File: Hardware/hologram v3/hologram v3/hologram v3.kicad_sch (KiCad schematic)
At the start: 706 parts, among them J1 Conn_01x06, J2 Conn_01x06_Socket, SW1 SW_Reset, SW2 SW_Boot, SW3 SW_OPT1, SW4 SW_OPT2, U1 SM16106SC, U10 SM16106SC, U11 SM16106SC, U12 SM16106SC, U13 SM16106SC, U14 SM16106SC, U15 SM16106SC, U16 SM16106SC, U17 SM16106SC, U18 SM16106SC, U19 SM16106SC, U2 SM16106SC, U20 SM16106SC, U21 SM16106SC, U22 SM16106SC, U23 SM16106SC, U24 SM16106SC, U25 SM16106SC, U26 SM16106SC, U27 SM16106SC, U28 SM16106SC, U29 SM16106SC, U3 SM16106SC, U30 SM16106SC, U31 SM16106SC, U32 SM16106SC, U33 ESP32-S3-WROOM-1(N16R8), U34 SY8286ARAC 12v->4v, U36 SY8286ARAC 12v->3.3v, U4 SM16106SC, U5 SM16106SC, U6 SM16106SC, U7 SM16106SC, U8 SM16106SC, U9 SM16106SC

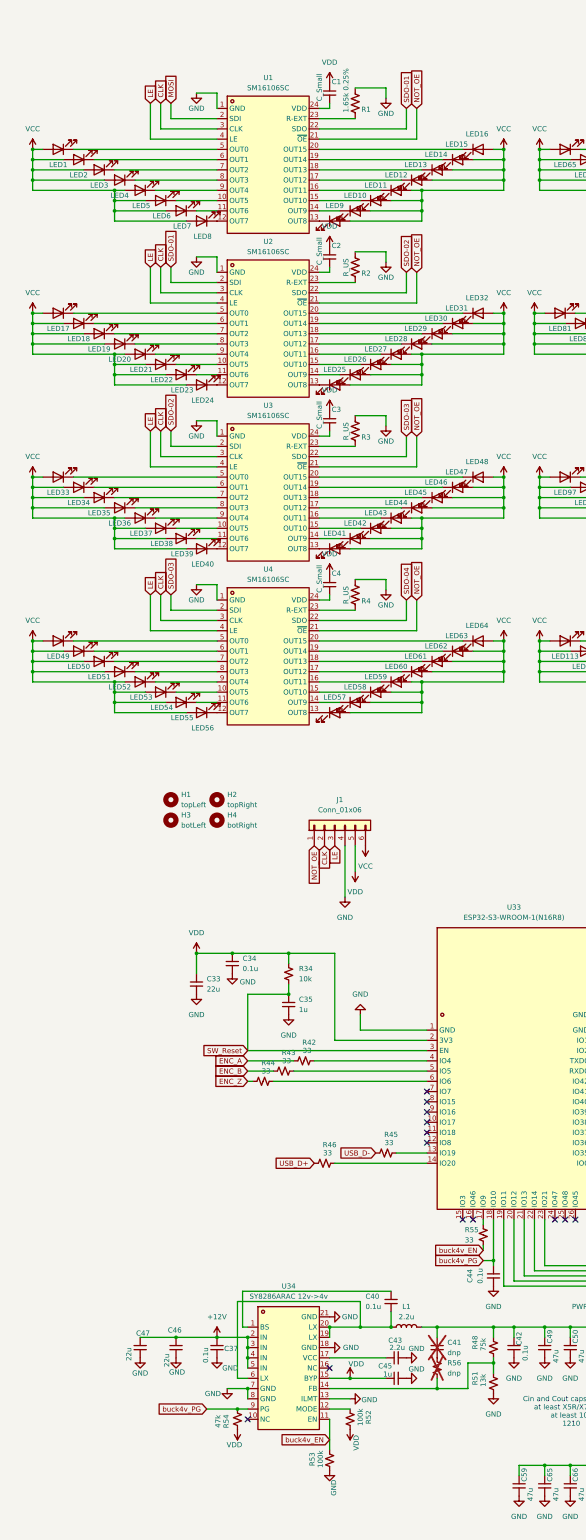
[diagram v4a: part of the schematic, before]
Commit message: updated hologram kicad to have all part nums and datasheet links. added screenshots of scematics for report
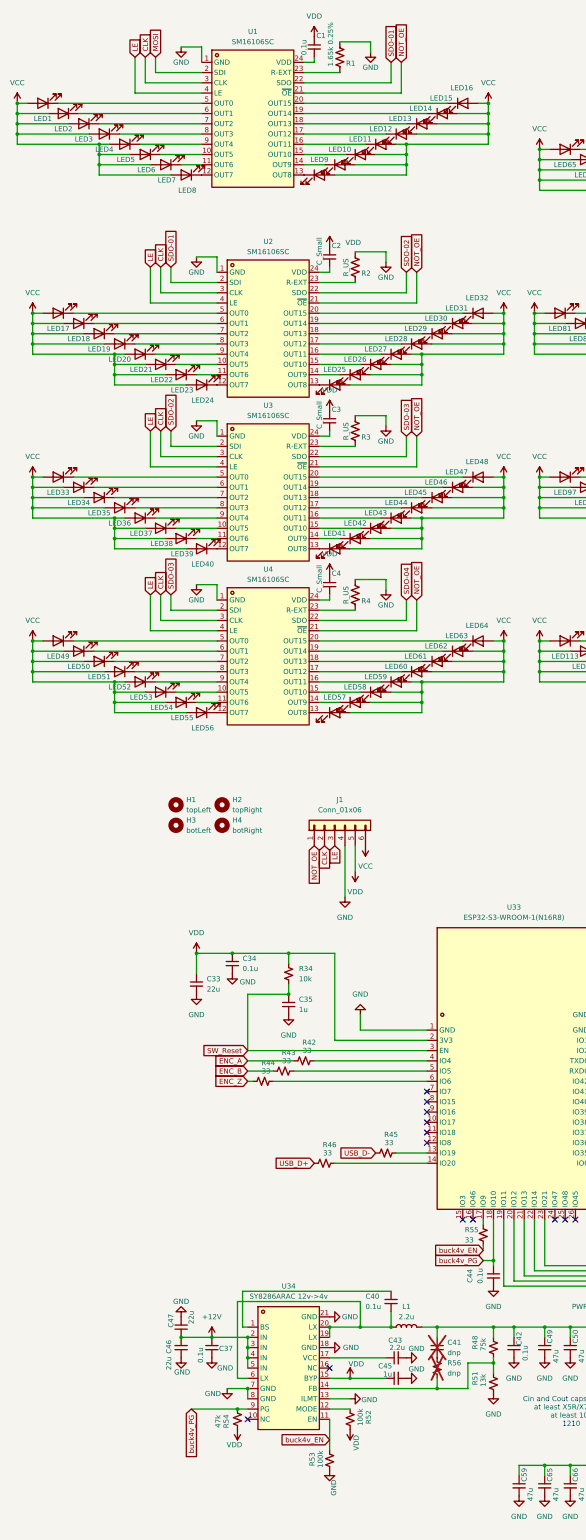
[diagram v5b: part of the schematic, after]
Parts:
- C1: value C_Small -> 0.1u; LCSC Part (none) -> C14663; Part Name (none) -> CC0603KRX7R9BB104
- C10, C11, C12, C13, C14, C15, C16, C17, C18, C19, C2, C20, C21, C22, C23, C24, C25, C26, C27, C28, C29, C3, C30, C31, C32, C4, C5, C6, C7, C8, C9: LCSC Part (none) -> C14663; Part Name (none) -> CC0603KRX7R9BB104
- C33: LCSC Part (none) -> C45783; Part Name (none) -> CL21A226MAQNNNE
- C34, C37, C38, C39, C40, C42, C44, C55, C56, C60: LCSC Part (none) -> C307331; Part Name (none) -> CL05B104KB54PNC
- C35, C45: LCSC Part (none) -> C59302; Part Name (none) -> 0603B105K250NT
- C36: LCSC Part (none) -> C440198; Part Name (none) -> GRM21BR61H106KE43L
- C43, C57: LCSC Part (none) -> C415535; Part Name (none) -> GRM188Z71E225KE43D
- C46, C47, C53, C54, C61, C62, C63, C64: LCSC Part (none) -> C2918511; Part Name (none) -> CS3225X7R226K250NRL
- C48: Part Name (none) -> MA25V100M6x6
- C49, C50, C51, C52, C59, C65, C66, C67: LCSC Part (none) -> C5440143; Part Name (none) -> CS3225X7R476K160NRL
- D1: LCSC Part (none) -> C82544; Part Name (none) -> 1N5819HW-7-F
- D10: LCSC Part (none) -> C2286; Part Name (none) -> KT-0603R
- D11: LCSC Part (none) -> C2287; Part Name (none) -> KT-0603Y
- D12: LCSC Part (none) -> C2288; Part Name (none) -> KT-0603B
- D2, D3, D4: LCSC Part (none) -> C5451650; Part Name (none) -> LESD5Z5.0CT1G-HXY
- D5, D6, D7, D8: Part Name (none) -> LESD5Z5.0CT1G
- D9: Part Name (none) -> SMBJ13A
- F1: LCSC Part C47002391 -> C47002391; Part Name (none) -> SMD1812-300C-30V
- J1: LCSC Part (none) -> C6332199; Part Name (none) -> HB-PH3-25416PB2GOP
- J2: LCSC Part (none) -> C5290371; Part Name (none) -> MX128-5.0-06P-GN01-Cu-Y-A
- L1: LCSC Part (none) -> C439019; Part Name (none) -> CMLO1040H2R2MTT
- L2: LCSC Part (none) -> C439021; Part Name (none) -> CMLO1040H4R7MTT
- LED1, LED10, LED100, LED101, LED102, LED103, LED104, LED105, LED106, LED107, LED108, LED109, LED11, LED110, LED111, LED112, LED113, LED114, LED115, LED116, LED117, LED118, LED119, LED12, LED120, LED121, LED122, LED123, LED124, LED125, LED126, LED127, LED128, LED129, LED13, LED130, LED131, LED132, LED133, LED134, LED135, LED136, LED137, LED138, LED139, LED14, LED140, LED141, LED142, LED143, LED144, LED145, LED146, LED147, LED148, LED149, LED15, LED150, LED151, LED152, LED153, LED154, LED155, LED156, LED157, LED158, LED159, LED16, LED160, LED161, LED162, LED163, LED164, LED165, LED166, LED167, LED168, LED169, LED17, LED170, LED171, LED172, LED173, LED174, LED175, LED176, LED177, LED178, LED179, LED18, LED180, LED181, LED182, LED183, LED184, LED185, LED186, LED187, LED188, LED189, LED19, LED190, LED191, LED192, LED193, LED194, LED195, LED196, LED197, LED198, LED199, LED2, LED20, LED200, LED201, LED202, LED203, LED204, LED205, LED206, LED207, LED208, LED209, LED21, LED210, LED211, LED212, LED213, LED214, LED215, LED216, LED217, LED218, LED219, LED22, LED220, LED221, LED222, LED223, LED224, LED225, LED226, LED227, LED228, LED229, LED23, LED230, LED231, LED232, LED233, LED234, LED235, LED236, LED237, LED238, LED239, LED24, LED240, LED241, LED242, LED243, LED244, LED245, LED246, LED247, LED248, LED249, LED25, LED250, LED251, LED252, LED253, LED254, LED255, LED256, LED257, LED258, LED259, LED26, LED260, LED261, LED262, LED263, LED264, LED265, LED266, LED267, LED268, LED269, LED27, LED270, LED271, LED272, LED273, LED274, LED275, LED276, LED277, LED278, LED279, LED28, LED280, LED281, LED282, LED283, LED284, LED285, LED286, LED287, LED288, LED289, LED29, LED290, LED291, LED292, LED293, LED294, LED295, LED296, LED297, LED298, LED299, LED3, LED30, LED300, LED301, LED302, LED303, LED304, LED305, LED306, LED307, LED308, LED309, LED31, LED310, LED311, LED312, LED313, LED314, LED315, LED316, LED317, LED318, LED319, LED32, LED320, LED321, LED322, LED323, LED324, LED325, LED326, LED327, LED328, LED329, LED33, LED330, LED331, LED332, LED333, LED334, LED335, LED336, LED337, LED338, LED339, LED34, LED340, LED341, LED342, LED343, LED344, LED345, LED346, LED347, LED348, LED349, LED35, LED350, LED351, LED352, LED353, LED354, LED355, LED356, LED357, LED358, LED359, LED36, LED360, LED361, LED362, LED363, LED364, LED365, LED366, LED367, LED368, LED369, LED37, LED370, LED371, LED372, LED373, LED374, LED375, LED376, LED377, LED378, LED379, LED38, LED380, LED381, LED382, LED383, LED384, LED385, LED386, LED387, LED388, LED389, LED39, LED390, LED391, LED392, LED393, LED394, LED395, LED396, LED397, LED398, LED399, LED4, LED40, LED400, LED401, LED402, LED403, LED404, LED405, LED406, LED407, LED408, LED409, LED41, LED410, LED411, LED412, LED413, LED414, LED415, LED416, LED417, LED418, LED419, LED42, LED420, LED421, LED422, LED423, LED424, LED425, LED426, LED427, LED428, LED429, LED43, LED430, LED431, LED432, LED433, LED434, LED435, LED436, LED437, LED438, LED439, LED44, LED440, LED441, LED442, LED443, LED444, LED445, LED446, LED447, LED448, LED449, LED45, LED450, LED451, LED452, LED453, LED454, LED455, LED456, LED457, LED458, LED459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: LCSC Part C2297 -> C5355441; Part Name (none) -> A-SC170ZB1D-A02-3T
- R1, R10, R11, R12, R13, R14, R15, R16, R17, R18, R19, R2, R20, R21, R22, R23, R24, R25, R26, R27, R28, R29, R3, R30, R31, R32, R4, R5, R6, R7, R8, R9: LCSC Part (none) -> C705743; Part Name (none) -> RT0603BRD071K65L
- R33: LCSC Part (none) -> C22935; Part Name (none) -> 0603WAF1004T5E
- R34, R41, R47, R62: LCSC Part (none) -> C5126214; Part Name (none) -> FRH0603B1002TS
- R35, R36: LCSC Part (none) -> C23186; Part Name (none) -> 0603WAF5101T5E
- R37, R38, R39: LCSC Part (none) -> C4190; Part Name (none) -> 0603WAF2201T5E
- R40, R52, R53, R58: LCSC Part (none) -> C25803; Part Name (none) -> 0603WAF1003T5E
- R42, R43, R44, R45, R46, R49, R50, R55, R65, R66: LCSC Part (none) -> C25105; Part Name (none) -> 0402WGF330JTCE
- R48: LCSC Part (none) -> C723587; Part Name (none) -> RT0603BRD0775KL
- R51: LCSC Part (none) -> C50670543; Part Name (none) -> TC0325B1302T5F
- R54, R63, R64: LCSC Part (none) -> C25819; Part Name (none) -> 0603WAF4702T5E
- R57: LCSC Part (none) -> C22843; Part Name (none) -> 0603WAF1501T5E
- R59: LCSC Part (none) -> C22765; Part Name (none) -> 0603WAF1201T5E
- R60: LCSC Part (none) -> C23138; Part Name (none) -> 0603WAF3300T5E
- R61: LCSC Part (none) -> C861415; Part Name (none) -> RT0603BRD0745K3L
- SW1, SW2, SW3, SW4: LCSC Part (none) -> C49234124; Part Name (none) -> HX 3x4x2-2P-1.6N TACTILE SWITCH
- TP1: now left out of the parts list
- U1, U10, U11, U12, U13, U14, U15, U16, U17, U18, U19, U2, U20, U21, U22, U23, U24, U25, U26, U27, U28, U29, U3, U30, U31, U32, U4, U5, U6, U7, U8, U9: Part Name (none) -> SM16206S
- U33: Part Name (none) -> ESP32-S3-WROOM-1-N16R8
- U34, U36: Part Name (none) -> SY8286ARAC
- U35: value ~ -> (none); Part Name (none) -> TYPE-C 16PIN 2MD(073)
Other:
- title: Hologram spinnig panel -> Hologram spinning panel
- moved on the sheet: C1, C37, C46, C47, H1, H2, H3, H4, LED1, LED10, LED11, LED12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
